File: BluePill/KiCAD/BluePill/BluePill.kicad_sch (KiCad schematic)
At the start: 7 parts, among them J1 Motor, J2 Encoder, J3 UART, J4 I2C, U1 BP

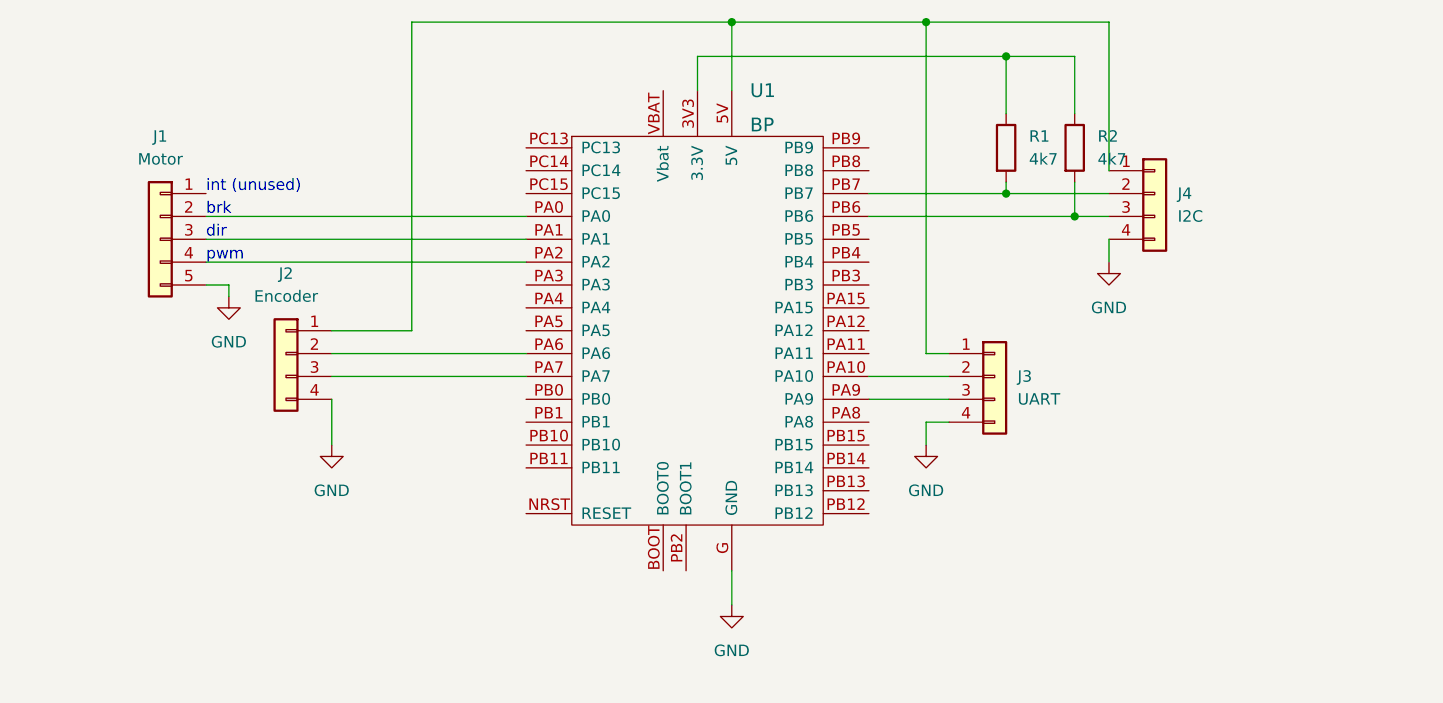
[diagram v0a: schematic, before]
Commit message: Actual schema (not a board)
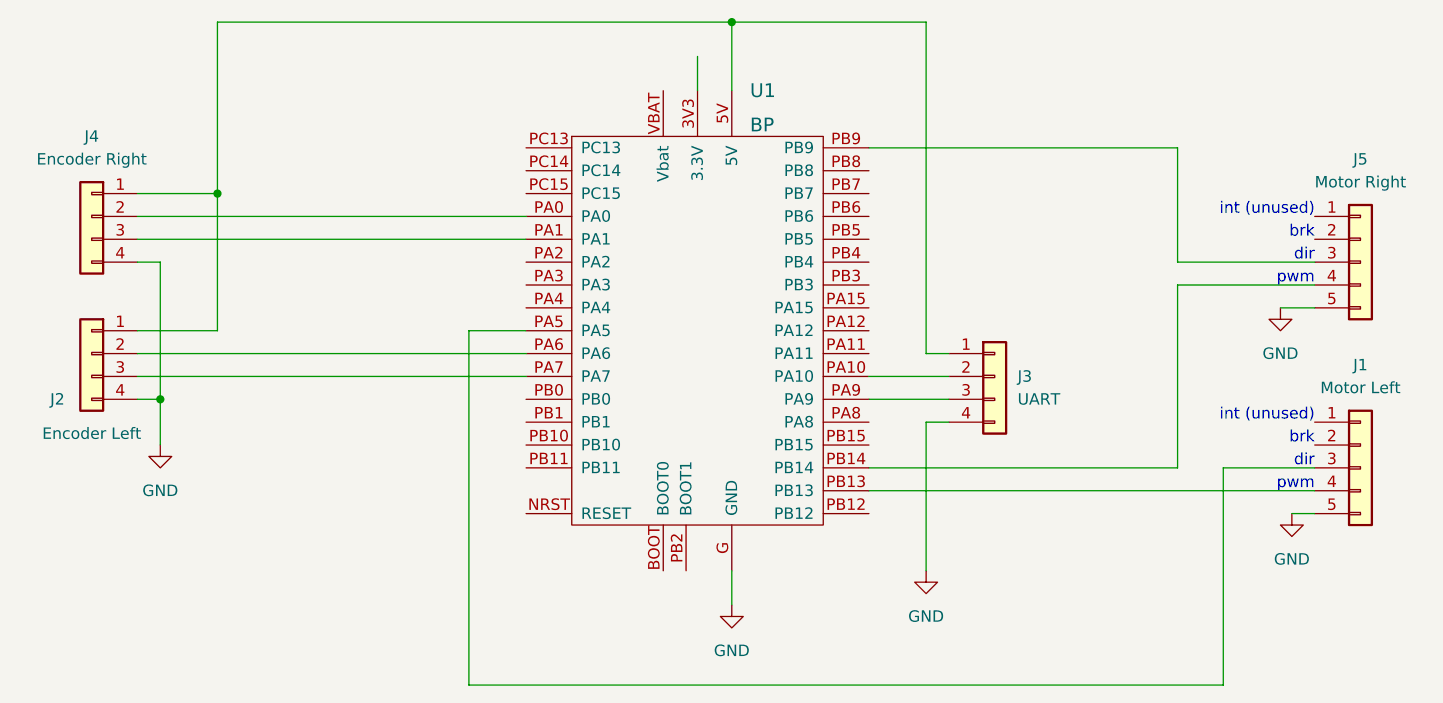
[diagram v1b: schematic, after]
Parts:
- removed R1, R2: 4k7, Resistor_THT:R_Axial_DIN0204_L3.6mm_D1.6mm_P2.54mm_Vertical, symbol Device:R
- added J5: Motor Right, Connector_PinHeader_2.54mm:PinHeader_1x05_P2.54mm_Vertical, symbol Connector_Generic:Conn_01x05
- J1: value Motor -> Motor Left
- J2: value Encoder -> Encoder Left
- J4: value I2C -> Encoder Right
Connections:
- net GND: now also J5.5 (Pin_5)
- net at J4.2 (Pin_2): now also U1.PA0; no longer U1.PB7
- net at J4.3 (Pin_3): now also U1.PA1; no longer U1.PB6
- net at J1.2 (Pin_2): no longer U1.PA0
- net at J1.3 (Pin_3): now also U1.PA5; no longer U1.PA1
- net at J1.4 (Pin_4): now also U1.PB13; no longer U1.PA2
- net at U1.PB14: now also J5.4 (Pin_4)
- net at U1.PB9: now also J5.3 (Pin_3)
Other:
- moved on the sheet: J1, J2, J4
